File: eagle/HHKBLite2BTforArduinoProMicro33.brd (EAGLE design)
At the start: 100 x 61 mm, 40 parts, among them CON1 45045-1445, CON2 45045-0845, IC1 4514N, IC2 4512N, IC4 HT7733A, J1 J7MM, J2 J15MM, J4 J10MM

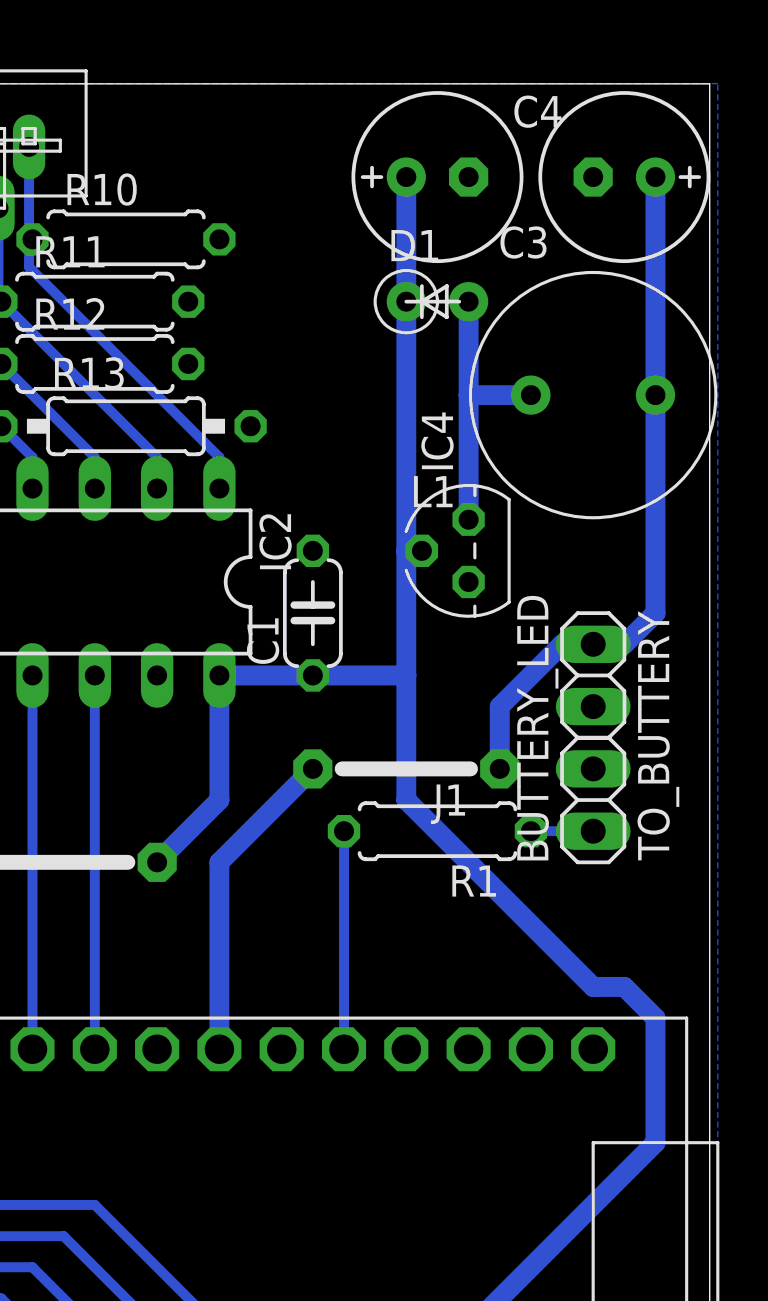
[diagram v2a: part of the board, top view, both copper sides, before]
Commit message: 入力ピンをINPUTからINPUT_PULLUPに変更
内部プルアップ抵抗を使うように書き換えた.
それに伴い, 該当箇所の真理値を逆転させた.
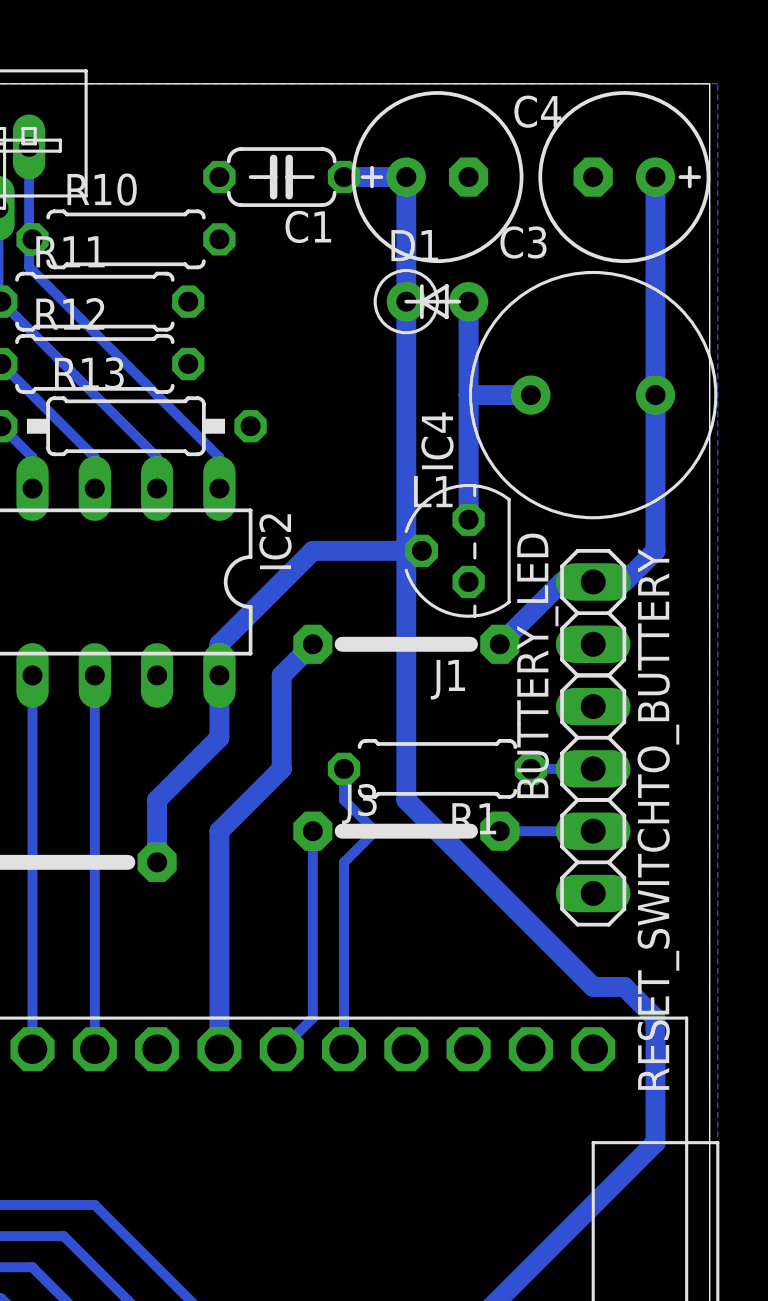
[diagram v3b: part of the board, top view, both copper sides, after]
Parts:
- added J3: J7MM, jumper:07
- added RESET_SWITCH: (no value), pinhead:1X02
- moved C1 17.8 mm to (82.5, 57.1), turned to 180 degrees
- moved J1 5.08 mm to (87.6, 38.1)
- moved R1 2.54 mm to (88.9, 33.0)
- moved BUTTERY_LED 2.54 mm to (95.2, 34.3)
- moved TO_BUTTERY 2.54 mm to (95.2, 39.4)
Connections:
- new net N$4: J3.2, RESET_SWITCH.1
- new net N$8: J3.1, U$2.7
- net GND: now also RESET_SWITCH.2
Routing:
- net N$8: track 0.00 -> 9.42 mm
- net +3V3: track 165.1 -> 170.5 mm
- net N$4: track 0.00 -> 3.81 mm
- net N$2: track 8.89 -> 12.5 mm
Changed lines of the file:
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@@
 <element name="CON1" library="5204" package="52045-1445" value="45045-1445" x="25.4" y="58.42" rot="R180"/>
 <element name="CON2" library="5204" package="52045-0845" value="45045-0845" x="63.5" y="55.88"/>
-<element name="TO_BUTTERY" library="pinhead" package="1X02" value="" x="95.25" y="36.83" rot="R270"/>
+<element name="TO_BUTTERY" library="pinhead" package="1X02" value="" x="95.25" y="39.37" rot="R270"/>
 <element name="R10" library="rcl" package="0207/7" value="10k" x="76.2" y="54.61"/>
 <element name="R11" library="rcl" package="0207/7" value="10k" x="74.93" y="52.07"/>
@@
 <element name="D15" library="diode" package="DO34-7" value="BAS15" x="12.7" y="33.02" rot="R270"/>
 <element name="D16" library="diode" package="DO34-7" value="BAS15" x="11.43" y="30.48" rot="R270"/>
-<element name="BUTTERY_LED" library="pinhead" package="1X02" value="" x="95.25" y="31.75" rot="R90"/>
-<element name="R1" library="rcl" package="0207/7" value="160" x="88.9" y="30.48" rot="R180"/>
+<element name="BUTTERY_LED" library="pinhead" package="1X02" value="" x="95.25" y="34.29" rot="R90"/>
+<element name="R1" library="rcl" package="0207/7" value="160" x="88.9" y="33.02" rot="R180"/>
 <element name="U$2" library="ArduinoProMicro" package="ARDUINO_PRO_MICRO" value="ARDUINO_PRO_MICRO" x="82.55" y="13.97" rot="R270"/>
-<element name="J1" library="jumper" package="07" value="J7MM" x="87.63" y="33.02" rot="R180"/>
+<element name="J1" library="jumper" package="07" value="J7MM" x="87.63" y="38.1" rot="R180"/>
 <element name="J2" library="jumper" package="15" value="J15MM" x="69.85" y="29.21"/>
 <element name="J4" library="jumper" package="10" value="J10MM" x="40.64" y="27.94" rot="R90"/>
-<element name="C1" library="rcl" package="C050-024X044" value="0.1uF" x="83.82" y="39.37" rot="R90"/>
+<element name="C1" library="rcl" package="C050-024X044" value="0.1uF" x="82.55" y="57.15" rot="R180"/>
+<element name="RESET_SWITCH" library="pinhead" package="1X02" value="" x="95.25" y="29.21" rot="R270"/>
+<element name="J3" library="jumper" package="07" value="J7MM" x="87.63" y="30.48"/>
 </elements>
 <signals>
@@
 <contactref element="J4" pad="1"/>
 <contactref element="J4" pad="2"/>
-<wire x1="33.02" y1="31.75" x2="36.48" y2="36.06" width="0" layer="19" extent="16-16"/>
+<contactref element="RESET_SWITCH" pad="2"/>
+<wire x1="36.48" y1="36.06" x2="33.02" y2="31.75" width="0" layer="19" extent="16-16"/>
 </signal>
 <signal name="N$3" class="2">
@@
 <contactref element="C3" pad="+"/>
 <contactref element="TO_BUTTERY" pad="1"/>
-<wire x1="95.25" y1="38.1" x2="96.52" y2="38.1" width="0.8128" layer="16"/>
-<wire x1="96.52" y1="38.1" x2="97.79" y2="39.37" width="0.8128" layer="16"/>
-<wire x1="95.25" y1="38.1" x2="93.98" y2="38.1" width="0.8128" layer="16"/>
 <contactref element="J1" pad="1"/>
-<wire x1="91.44" y1="33.02" x2="91.44" y2="35.56" width="0.8128" layer="16"/>
-<wire x1="91.44" y1="35.56" x2="93.98" y2="38.1" width="0.8128" layer="16"/>
 <contactref element="L1" pad="+"/>
 <wire x1="97.79" y1="57.15" x2="97.79" y2="48.26" width="0.8128" layer="16"/>
-<wire x1="97.79" y1="48.26" x2="97.79" y2="39.37" width="0.8128" layer="16"/>
 <contactref element="J1" pad="2"/>
 <contactref element="U$2" pad="6"/>
-<wire x1="83.82" y1="33.02" x2="91.44" y2="33.02" width="0" layer="19" extent="1-1"/>
-<wire x1="83.82" y1="33.02" x2="80.01" y2="29.21" width="0.8128" layer="16"/>
-<wire x1="80.01" y1="29.21" x2="80.01" y2="21.59" width="0.8128" layer="16"/>
+<wire x1="95.25" y1="40.64" x2="93.98" y2="40.64" width="0.8128" layer="16"/>
+<wire x1="93.98" y1="40.64" x2="91.44" y2="38.1" width="0.8128" layer="16"/>
+<wire x1="95.25" y1="40.64" x2="96.52" y2="40.64" width="0.8128" layer="16"/>
+<wire x1="96.52" y1="40.64" x2="97.79" y2="41.91" width="0.8128" layer="16"/>
+<wire x1="97.79" y1="41.91" x2="97.79" y2="48.26" width="0.8128" layer="16"/>
+<wire x1="83.82" y1="38.1" x2="82.55" y2="36.83" width="0.8128" layer="16"/>
+<wire x1="82.55" y1="36.83" x2="82.55" y2="33.02" width="0.8128" layer="16"/>
+<wire x1="82.55" y1="33.02" x2="80.01" y2="30.48" width="0.8128" layer="16"/>
+<wire x1="80.01" y1="30.48" x2="80.01" y2="21.59" width="0.8128" layer="16"/>
+<wire x1="83.82" y1="38.1" x2="91.44" y2="38.1" width="0" layer="19" extent="1-1"/>
 </signal>
 <signal name="N$49">
@@
 <wire x1="33.02" y1="3.81" x2="86.36" y2="3.81" width="0.8128" layer="16"/>
 <contactref element="J2" pad="2"/>
-<wire x1="80.01" y1="36.83" x2="80.01" y2="31.75" width="0.8128" layer="16"/>
-<wire x1="80.01" y1="31.75" x2="77.47" y2="29.21" width="0.8128" layer="16"/>
 <wire x1="86.36" y1="3.81" x2="87.63" y2="5.08" width="0.8128" layer="16"/>
 <wire x1="87.63" y1="5.08" x2="87.63" y2="6.35" width="0.8128" layer="16"/>
 <contactref element="C1" pad="1"/>
-<wire x1="87.63" y1="57.15" x2="87.63" y2="52.07" width="0.8128" layer="16"/>
-<wire x1="80.01" y1="36.83" x2="83.82" y2="36.83" width="0.8128" layer="16"/>
 <contactref element="U$1" pad="11"/>
 <contactref element="J2" pad="1"/>
 <wire x1="49.88" y1="39.46" x2="51.98" y2="39.46" width="0.8128" layer="16"/>
 <wire x1="51.98" y1="39.46" x2="62.23" y2="29.21" width="0.8128" layer="16"/>
-<wire x1="87.63" y1="52.07" x2="87.63" y2="41.91" width="0.8128" layer="16"/>
 <wire x1="87.63" y1="41.91" x2="88.265" y2="41.91" width="0.8128" layer="16"/>
-<wire x1="87.63" y1="41.91" x2="87.63" y2="36.83" width="0.8128" layer="16"/>
-<wire x1="87.63" y1="36.83" x2="83.82" y2="36.83" width="0.8128" layer="16"/>
 <wire x1="87.63" y1="6.35" x2="87.63" y2="7.62" width="0.8128" layer="16"/>
 <wire x1="87.63" y1="7.62" x2="97.79" y2="17.78" width="0.8128" layer="16"/>
@@
 <wire x1="96.52" y1="24.13" x2="95.25" y2="24.13" width="0.8128" layer="16"/>
 <wire x1="95.25" y1="24.13" x2="87.63" y2="31.75" width="0.8128" layer="16"/>
-<wire x1="87.63" y1="31.75" x2="87.63" y2="36.83" width="0.8128" layer="16"/>
+<wire x1="80.01" y1="36.83" x2="80.01" y2="34.29" width="0.8128" layer="16"/>
+<wire x1="80.01" y1="34.29" x2="77.47" y2="31.75" width="0.8128" layer="16"/>
+<wire x1="77.47" y1="31.75" x2="77.47" y2="29.21" width="0.8128" layer="16"/>
+<wire x1="80.01" y1="36.83" x2="80.01" y2="38.1" width="0.8128" layer="16"/>
+<wire x1="80.01" y1="38.1" x2="83.82" y2="41.91" width="0.8128" layer="16"/>
+<wire x1="83.82" y1="41.91" x2="87.63" y2="41.91" width="0.8128" layer="16"/>
+<wire x1="87.63" y1="31.75" x2="87.63" y2="41.91" width="0.8128" layer="16"/>
+<wire x1="85.09" y1="57.15" x2="87.63" y2="57.15" width="0.8128" layer="16"/>
+<wire x1="87.63" y1="57.15" x2="87.63" y2="52.07" width="0.8128" layer="16"/>
+<wire x1="87.63" y1="52.07" x2="87.63" y2="41.91" width="0.8128" layer="16"/>
 <wire x1="77.47" y1="29.21" x2="62.23" y2="29.21" width="0" layer="19" extent="1-1"/>
 </signal>
@@
 <contactref element="BUTTERY_LED" pad="1"/>
 <contactref element="R1" pad="1"/>
-<wire x1="92.71" y1="30.48" x2="95.25" y2="30.48" width="0.4064" layer="16"/>
+<wire x1="92.71" y1="33.02" x2="95.25" y2="33.02" width="0.4064" layer="16"/>
 </signal>
 <signal name="N$2">
 <contactref element="U$2" pad="8"/>
 <contactref element="R1" pad="2"/>
-<wire x1="85.09" y1="30.48" x2="85.09" y2="21.59" width="0.4064" layer="16"/>
+<wire x1="85.09" y1="33.02" x2="85.09" y2="31.75" width="0.4064" layer="16"/>
+<wire x1="85.09" y1="31.75" x2="86.36" y2="30.48" width="0.4064" layer="16"/>
+<wire x1="86.36" y1="30.48" x2="85.09" y2="29.21" width="0.4064" layer="16"/>
+<wire x1="85.09" y1="29.21" x2="85.09" y2="21.59" width="0.4064" layer="16"/>
 </signal>
 <signal name="N$5">
@@
 <wire x1="36.32" y1="38.1" x2="36.48" y2="38.26" width="0.4064" layer="16"/>
 </signal>
+<signal name="N$4">
+<contactref element="RESET_SWITCH" pad="1"/>
+<contactref element="J3" pad="2"/>
+<wire x1="91.44" y1="30.48" x2="95.25" y2="30.48" width="0.4064" layer="16"/>
+</signal>
+<signal name="N$8">
+<contactref element="U$2" pad="7"/>
+<contactref element="J3" pad="1"/>
+<wire x1="83.82" y1="30.48" x2="83.82" y2="22.86" width="0.4064" layer="16"/>
+<wire x1="83.82" y1="22.86" x2="82.55" y2="21.59" width="0.4064" layer="16"/>
+</signal>
 </signals>

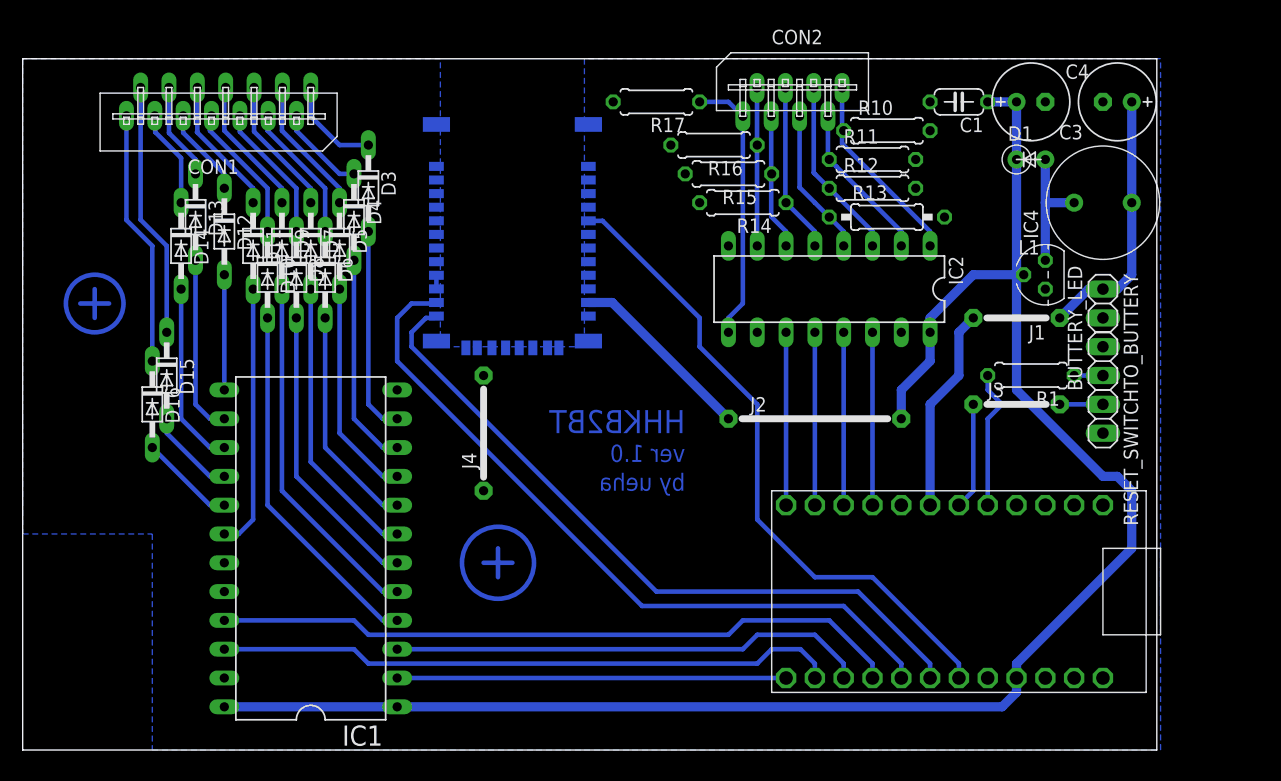
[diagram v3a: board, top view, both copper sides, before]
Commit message: Arduino IDE 1.6.x のためにいろいろ変更.
Arduino IDE 1.6.x と Arduino-Makefile でこのプロジェクトをコンパイルできるように
するために, いろいろいじった.
まだ試験的なものなので, 今回変更した Makefile を参考にし, 他のものも
書き換えると良い.
あと, ProMicro33 に関して言えば, これをそのまま使ってもコンパイルできない.
SparkFun から適切なボードコンフィグを持ってきて, 適切な場所に置き,
適切に Makefile を書き換える必要がある.
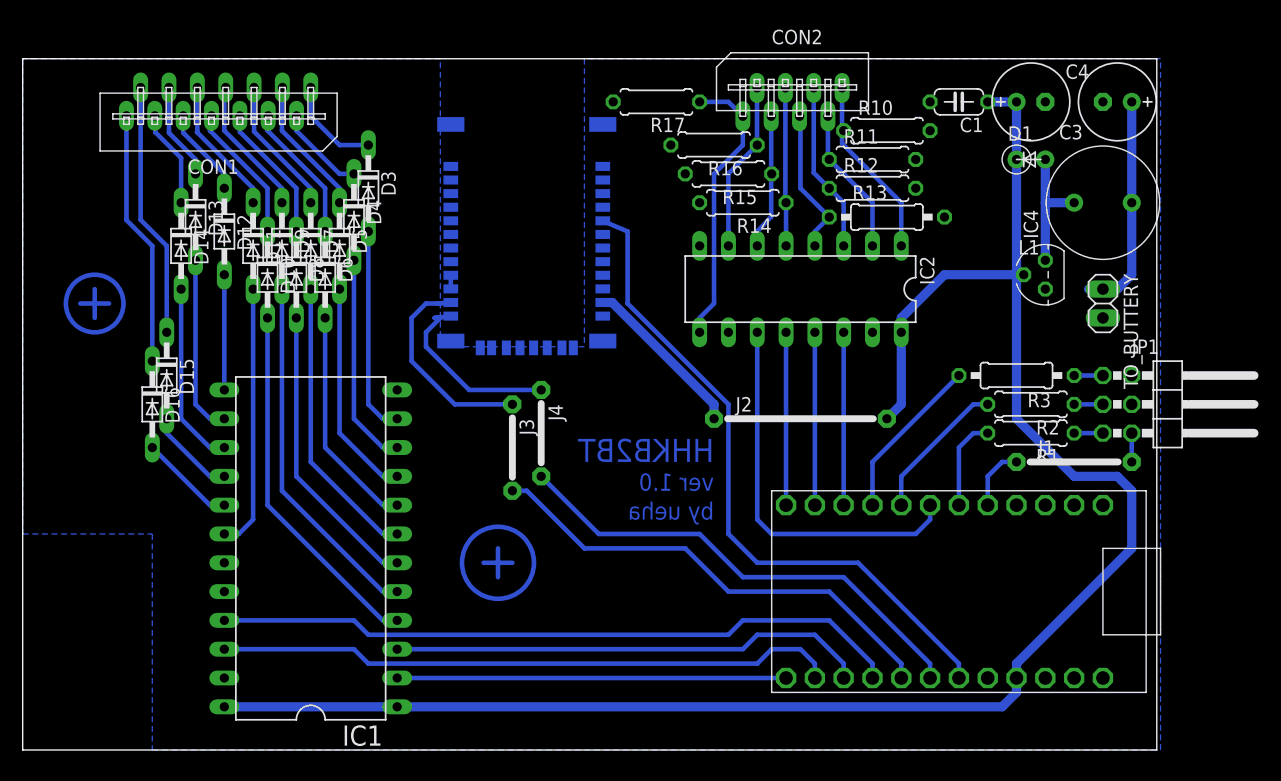
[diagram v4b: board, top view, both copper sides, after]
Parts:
- removed BUTTERY_LED, RESET_SWITCH: (no value), pinhead:1X02
- added JP1: (no value), pinhead:2X03/90
- added R2: 160, rcl:0207/7
- added R3: 160, rcl:0207/10
- J1: value J7MM -> J10MM; device jumper:07 -> jumper:10
- J4: value J10MM -> J7MM; device jumper:10 -> jumper:07
- moved J3 44.6 mm to (43.2, 26.7), turned to 270 degrees
- moved J1 13.7 mm to (92.7, 25.4), turned to 0 degrees
- moved R1 5.08 mm to (88.9, 27.9)
- moved J4 5.08 mm to (45.7, 27.9), turned to 270 degrees
- moved IC2 2.54 mm to (68.6, 40.6)
- moved U$1 1.27 mm to (44.5, 48.3)
- moved J2 1.27 mm to (68.6, 29.2)
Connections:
- new net N$10: JP1.3, R2.1
- new net N$11: JP1.5, R1.1
- new net N$12: J1.2, JP1.6
- new net N$13: J1.1, U$2.8
- new net N$14: J4.1, U$1.13
- new net N$18: J4.2, U$2.19
- net GND: now also JP1.2, JP1.4; no longer BUTTERY_LED.2, J4.1, J4.2, RESET_SWITCH.2
- net N$1: now also R3.2, U$2.4; no longer BUTTERY_LED.1, R1.1
- net N$16: now also U$2.1; no longer U$2.2
- net N$17: now also U$2.2; no longer U$2.3
- net N$2: now also U$2.7; no longer U$2.8
- net N$22: now also U$2.6; no longer U$2.1
- net N$4: now also R2.2, U$2.5; no longer J3.2, RESET_SWITCH.1
- net N$5: now also J3.1; no longer U$2.20
- net N$7: now also J3.2, U$2.20; no longer U$1.13, U$2.19
- net N$8: now also JP1.1, R3.1; no longer J3.1, U$2.7
- net N$9: now also U$2.3; no longer U$2.4
- net VCC_SRC: no longer J1.1, J1.2, U$2.6
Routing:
- net N$5: track 64.6 -> 18.5 mm
- net N$18: track 0.00 -> 42.4 mm
- net VCC_SRC: track 41.3 -> 19.6 mm
- net N$7: track 62.6 -> 41.9 mm
- net N$22: track 15.2 -> 34.1 mm
- net N$14: track 0.00 -> 16.8 mm
- net N$1: track 2.54 -> 15.9 mm
- net N$4: track 3.81 -> 12.8 mm
- net N$8: track 9.42 -> 2.54 mm
- net N$13: track 0.00 -> 5.61 mm
- net N$2: track 12.5 -> 8.15 mm
- net N$11: track 0.00 -> 2.54 mm
- net N$10: track 0.00 -> 2.54 mm
- net N$12: track 0.00 -> 2.54 mm
- net CON2BUS_D6: track 14.0 -> 16.3 mm
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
